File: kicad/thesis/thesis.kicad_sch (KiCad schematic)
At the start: 31 parts, among them J1 Conn_01x01_Socket, J10 Conn_01x01_Socket, J2 Conn_01x01_Socket, J3 Conn_01x07_Socket, J4 Conn_01x04_Socket, J5 Conn_01x01_Socket, J6 Conn_01x01_Socket, J7 Conn_01x01_Socket, J8 Conn_01x01_Socket, J9 Conn_01x03_Socket, Q1 IRLZB8721, U1 INA219AxD

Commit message: Added 5 pins for 3.3 and GND
Also added folder for pcb printed under thesis gerber
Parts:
- removed J2: Conn_01x01_Socket, Connector_PinSocket_2.54mm:PinSocket_1x01_P2.54mm_Vertical, symbol Connector:Conn_01x01_Socket
- added J11, J2: Conn_01x05_Socket, Connector_PinSocket_2.54mm:PinSocket_1x05_P2.54mm_Vertical, symbol Connector:Conn_01x05_Socket
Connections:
- net +3.3V: now also J11.1 (Pin_1), J11.2 (Pin_2), J11.3 (Pin_3), J11.4 (Pin_4), J11.5 (Pin_5)
- net GND: now also J2.1 (Pin_1), J2.2 (Pin_2), J2.3 (Pin_3), J2.4 (Pin_4), J2.5 (Pin_5)

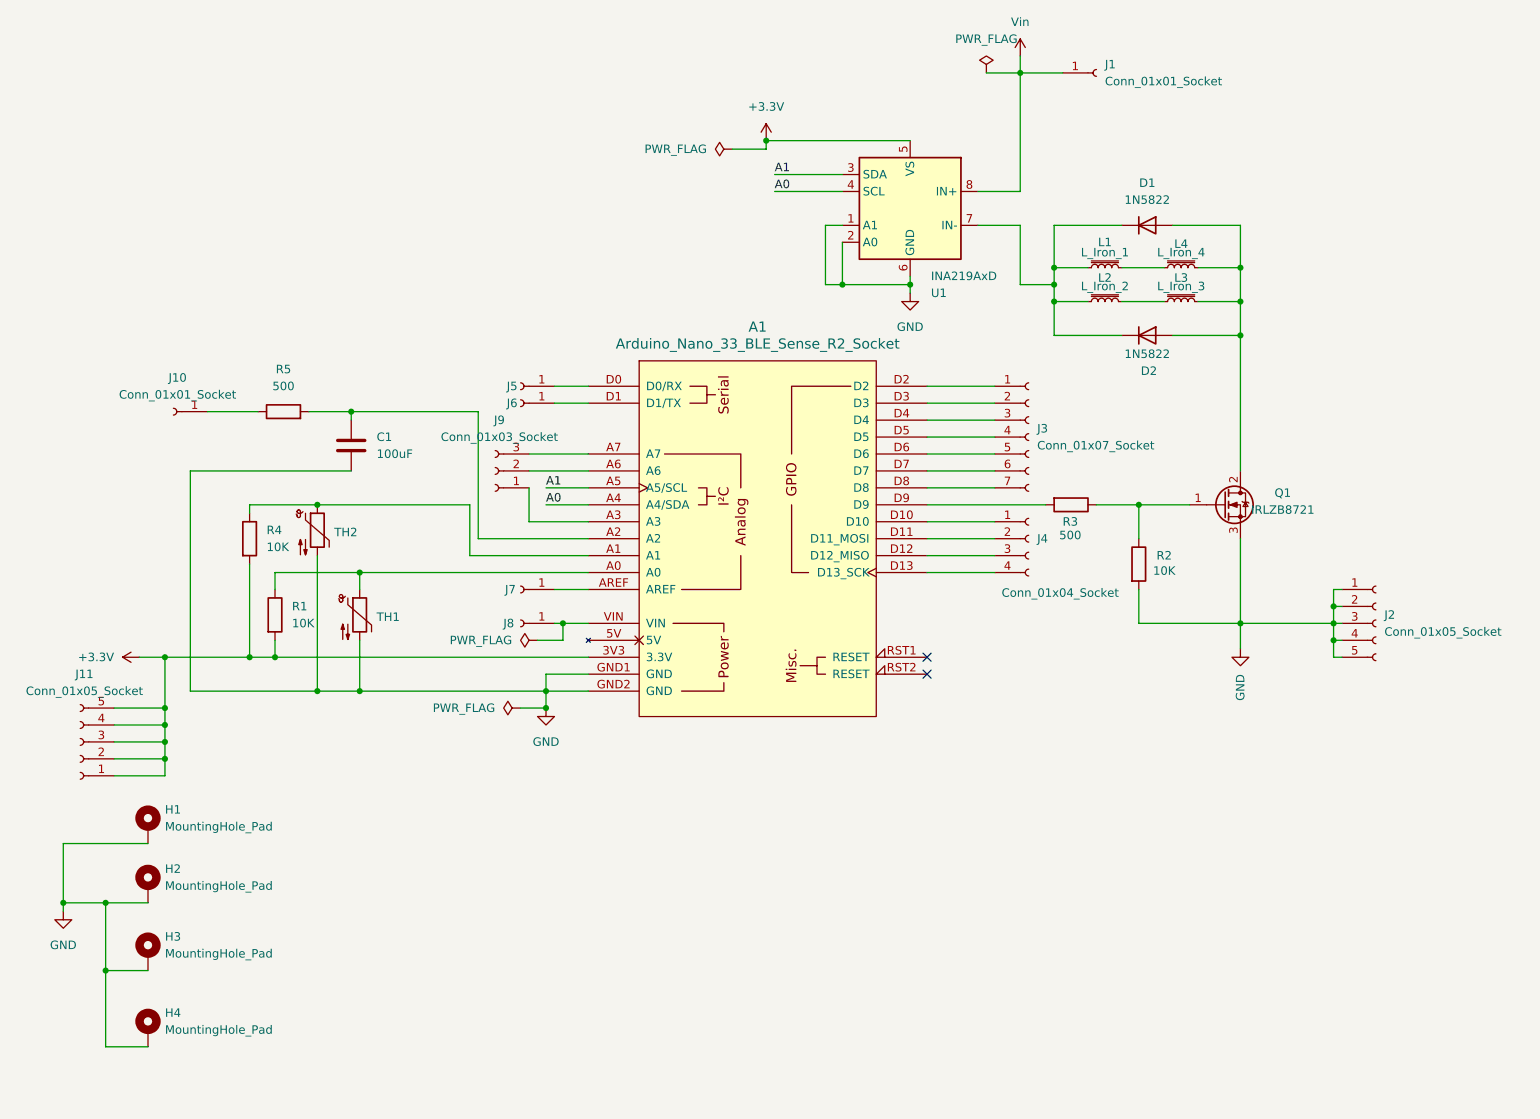
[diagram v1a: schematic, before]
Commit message: Updated PCB
fixed INA and change electromagnet orientation and fixed pin placement
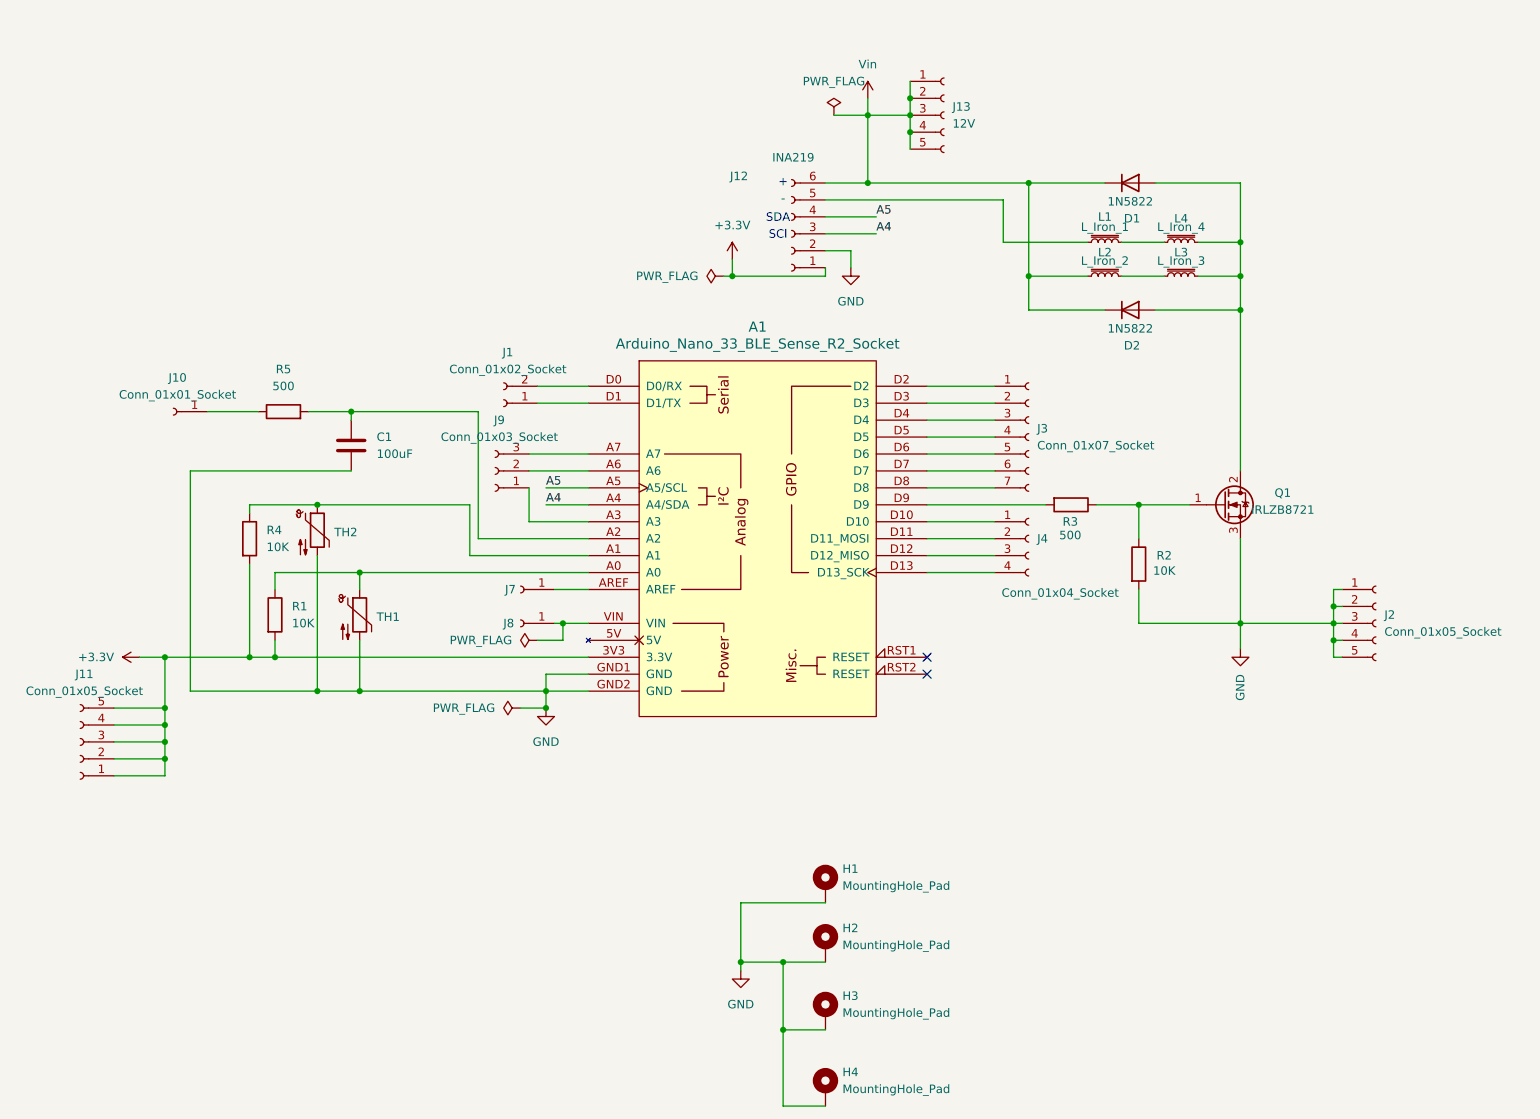
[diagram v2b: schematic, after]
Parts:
- removed J1, J5, J6: Conn_01x01_Socket, Connector_PinSocket_2.54mm:PinSocket_1x01_P2.54mm_Vertical, symbol Connector:Conn_01x01_Socket
- removed U1: INA219AxD, Connector_PinSocket_2.54mm:PinSocket_1x08_P2.54mm_Vertical, symbol Sensor_Energy:INA219AxD
- added J1: Conn_01x02_Socket, Connector_PinSocket_2.54mm:PinSocket_1x02_P2.54mm_Vertical, symbol Connector:Conn_01x02_Socket
- added J12: INA219, Connector_PinSocket_2.54mm:PinSocket_1x06_P2.54mm_Vertical, symbol Connector:Conn_01x06_Socket
- added J13: 12V, Connector_PinSocket_2.54mm:PinSocket_1x05_P2.54mm_Vertical, symbol Connector:Conn_01x05_Socket
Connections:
- net +3.3V: now also J12.1 (Pin_1)
- net GND: now also J12.2 (Pin_2)
- net Vin: now also D1.1 (K), D2.1 (K), L2.1, J12.6 (Pin_6), J13.1 (Pin_1), J13.2 (Pin_2), J13.3 (Pin_3), J13.4 (Pin_4), J13.5 (Pin_5)
- net at A1.D0 (D0/RX): now also J1.2 (Pin_2)
- net at A1.D1 (D1/TX): now also J1.1 (Pin_1)
- net A0 renamed A4
- net A4: now also J12.3 (Pin_3)
- net A1 renamed A5
- net A5: now also J12.4 (Pin_4)
- new net: J12.5 (Pin_5), L1.1
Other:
- note added: "+"
- note added: "-"
- note added: "SCl"
- note added: "SDA"
- moved on the sheet: H1, H2, H3, H4, L1, L2, L3, L4

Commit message: change diode length
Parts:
- D1, D2: footprint Diode_THT:D_DO-201AD_P12.70mm_Horizontal -> Diode_THT:D_DO-201AD_P15.24mm_Horizontal
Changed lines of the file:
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@@
 			)
 		)
-		(property "Footprint" "Diode_THT:D_DO-201AD_P12.70mm_Horizontal"
+		(property "Footprint" "Diode_THT:D_DO-201AD_P15.24mm_Horizontal"
 			(at 185.42 76.2 0)
 			(hide yes)
@@
 			)
 		)
-		(property "Footprint" "Diode_THT:D_DO-201AD_P12.70mm_Horizontal"
+		(property "Footprint" "Diode_THT:D_DO-201AD_P15.24mm_Horizontal"
 			(at 185.42 57.15 0)
 			(hide yes)

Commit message: Fixed the Terminal and track width fixes
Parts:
- removed L3: L_Iron_3, TerminalBlock_Phoenix:TerminalBlock_Phoenix_MKDS-1,5-2-5.08_1x02_P5.08mm_Horizontal, symbol Device:L_Iron_Small
- removed L4: L_Iron_4, TerminalBlock_Phoenix:TerminalBlock_Phoenix_MKDS-1,5-2-5.08_1x02_P5.08mm_Horizontal, symbol Device:L_Iron_Small
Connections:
- net at D1.2 (A), D2.2 (A), Q1.2 (D): now also L1.2, L2.2
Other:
- moved on the sheet: L1
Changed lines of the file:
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@@
 	)
 	(junction
-		(at 201.93 66.04)
-		(diameter 0)
-		(color 0 0 0 0)
-	)
-	(junction
 		(at 152.4 46.99)
 		(diameter 0)
@@
 	)
 	(junction
+		(at 201.93 66.04)
+		(diameter 0)
+		(color 0 0 0 0)
+	)
+	(junction
 		(at 57.15 128.27)
 		(diameter 0)
@@
 	(wire
 		(pts
-			(xy 166.37 66.04) (xy 179.07 66.04)
+			(xy 166.37 66.04) (xy 191.77 66.04)
 		)
 		(stroke
@@
 	(wire
 		(pts
-			(xy 97.79 102.87) (xy 104.14 102.87)
+			(xy 196.85 66.04) (xy 201.93 66.04)
 		)
 		(stroke
@@
 	(wire
 		(pts
-			(xy 195.58 66.04) (xy 201.93 66.04)
+			(xy 97.79 102.87) (xy 104.14 102.87)
 		)
 		(stroke
@@
 	(wire
 		(pts
-			(xy 184.15 71.12) (xy 190.5 71.12)
-		)
-		(stroke
-			(width 0)
-			(type default)
-		)
-	)
-	(wire
-		(pts
 			(xy 57.15 115.57) (xy 57.15 118.11)
 		)
@@
 	(wire
 		(pts
-			(xy 195.58 71.12) (xy 201.93 71.12)
-		)
-		(stroke
-			(width 0)
-			(type default)
-		)
-	)
-	(wire
-		(pts
 			(xy 154.94 90.17) (xy 165.1 90.17)
 		)
@@
 	(wire
 		(pts
+			(xy 184.15 71.12) (xy 201.93 71.12)
+		)
+		(stroke
+			(width 0)
+			(type default)
+		)
+	)
+	(wire
+		(pts
 			(xy 154.94 113.03) (xy 165.1 113.03)
 		)
@@
 	(wire
 		(pts
-			(xy 184.15 66.04) (xy 190.5 66.04)
-		)
-		(stroke
-			(width 0)
-			(type default)
-		)
-	)
-	(wire
-		(pts
 			(xy 133.35 195.58) (xy 133.35 184.15)
 		)
@@
 	)
 	(symbol
-		(lib_id "Device:L_Iron_Small")
-		(at 193.04 71.12 90)
-		(unit 1)
-		(body_style 1)
-		(exclude_from_sim no)
-		(in_bom yes)
-		(on_board yes)
-		(in_pos_files yes)
-		(dnp no)
-		(property "Reference" "L3"
-			(at 193.04 67.564 90)
-			(show_name no)
-			(do_not_autoplace no)
-			(effects
-				(font
-					(size 1.27 1.27)
-				)
-			)
-		)
-		(property "Value" "L_Iron_3"
-			(at 193.04 68.834 90)
-			(show_name no)
-			(do_not_autoplace no)
-			(effects
-				(font
-					(size 1.27 1.27)
-				)
-			)
-		)
-		(property "Footprint" "TerminalBlock_Phoenix:TerminalBlock_Phoenix_MKDS-1,5-2-5.08_1x02_P5.08mm_Horizontal"
-			(at 193.04 71.12 0)
-			(hide yes)
-			(show_name no)
-			(do_not_autoplace no)
-			(effects
-				(font
-					(size 1.27 1.27)
-				)
-			)
-		)
-		(property "Datasheet" ""
-			(at 193.04 71.12 0)
-			(hide yes)
-			(show_name no)
-			(do_not_autoplace no)
-			(effects
-				(font
-					(size 1.27 1.27)
-				)
-			)
-		)
-		(property "Description" "Inductor with iron core, small symbol"
-			(at 193.04 71.12 0)
-			(hide yes)
-			(show_name no)
-			(do_not_autoplace no)
-			(effects
-				(font
-					(size 1.27 1.27)
-				)
-			)
-		)
-		(pin "2"
-		)
-		(pin "1"
-		)
-		(instances
-			(project "thesis"
-				(path "/4ebb0c45-f912-48a8-89a3-8cdd50b81c57"
-					(reference "L3")
-					(unit 1)
-				)
-			)
-		)
-	)
-	(symbol
 		(lib_id "Connector:Conn_01x05_Socket")
 		(at 157.48 46.99 0)
@@
 	)
 	(symbol
-		(lib_id "Device:L_Iron_Small")
-		(at 193.04 66.04 90)
-		(unit 1)
-		(body_style 1)
-		(exclude_from_sim no)
-		(in_bom yes)
-		(on_board yes)
-		(in_pos_files yes)
-		(dnp no)
-		(property "Reference" "L4"
-			(at 193.04 62.484 90)
-			(show_name no)
-			(do_not_autoplace no)
-			(effects
-				(font
-					(size 1.27 1.27)
-				)
-			)
-		)
-		(property "Value" "L_Iron_4"
-			(at 193.04 63.754 90)
-			(show_name no)
-			(do_not_autoplace no)
-			(effects
-				(font
-					(size 1.27 1.27)
-				)
-			)
-		)
-		(property "Footprint" "TerminalBlock_Phoenix:TerminalBlock_Phoenix_MKDS-1,5-2-5.08_1x02_P5.08mm_Horizontal"
-			(at 193.04 66.04 0)
-			(hide yes)
-			(show_name no)
-			(do_not_autoplace no)
-			(effects
-				(font
-					(size 1.27 1.27)
-				)
-			)
-		)
-		(property "Datasheet" ""
-			(at 193.04 66.04 0)
-			(hide yes)
-			(show_name no)
-			(do_not_autoplace no)
-			(effects
-				(font
-					(size 1.27 1.27)
-				)
-			)
-		)
-		(property "Description" "Inductor with iron core, small symbol"
-			(at 193.04 66.04 0)
-			(hide yes)
-			(show_name no)
-			(do_not_autoplace no)
-			(effects
-				(font
-					(size 1.27 1.27)
-				)
-			)
-		)
-		(pin "2"
-		)
-		(pin "1"
-		)
-		(instances
-			(project "thesis"
-				(path "/4ebb0c45-f912-48a8-89a3-8cdd50b81c57"
-					(reference "L4")
-					(unit 1)
-				)
-			)
-		)
-	)
-	(symbol
 		(lib_id "Mechanical:MountingHole_Pad")
 		(at 139.7 181.61 0)
@@
 	(symbol
 		(lib_id "Device:L_Iron_Small")
-		(at 181.61 66.04 90)
+		(at 194.31 66.04 90)
 		(unit 1)
 		(body_style 1)
@@
 		(dnp no)
 		(property "Reference" "L1"
-			(at 181.61 62.23 90)
+			(at 194.31 62.23 90)
 			(show_name no)
 			(do_not_autoplace no)
@@
 		)
 		(property "Value" "L_Iron_1"
-			(at 181.61 63.754 90)
+			(at 194.31 63.754 90)
 			(show_name no)
 			(do_not_autoplace no)
@@
 		)
 		(property "Footprint" "TerminalBlock_Phoenix:TerminalBlock_Phoenix_MKDS-1,5-2-5.08_1x02_P5.08mm_Horizontal"
-			(at 181.61 66.04 0)
+			(at 194.31 66.04 0)
 			(hide yes)
 			(show_name no)
@@
 		)
 		(property "Datasheet" ""
-			(at 181.61 66.04 0)
+			(at 194.31 66.04 0)
 			(hide yes)
 			(show_name no)
@@
 		)
 		(property "Description" "Inductor with iron core, small symbol"
-			(at 181.61 66.04 0)
+			(at 194.31 66.04 0)
 			(hide yes)
 			(show_name no)
